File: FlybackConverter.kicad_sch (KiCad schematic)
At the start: 42 parts, among them J1 USB_C_Receptacle_PowerOnly_6P, T1 Transformer_1P_2S, U1 LNK6428K, U2 TPS25820DSST

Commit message: 2024/11/15
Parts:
- removed U1: LNK6428K, Package_SO:PowerIntegrations_eSOP-12B, symbol Regulator_Switching:LNK626PG
- added U1: TNY278G, Package_DIP:PowerIntegrations_SMD-8C, symbol Regulator_Switching:TNY278G
- added VR4: P6KE150A, Diode_THT:D_DO-15_P10.16mm_Horizontal, symbol Device:D_Zener
- C6: value 470p -> 10nF
- R11: value 200k -> 1k
- R3: value 150 -> 100
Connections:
- net PRI: now also VR4.2 (A); no longer R11.1
- net at R6.2, R7.1, TP4.1: now also U1.1 (EN/UV)
- net at C2.2, C7.2, C8.2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: now also U1.5 (S), U1.6 (S), U1.7 (S), U1.8 (S)
- net at D2.1 (K), R3.2: now also R11.2
- net at D2.2 (A), T1.7 (AB): now also U1.4 (D)
- net at C6.2, R3.1: no longer R11.2
- net at C7.1, R8.1: now also U1.2 (BP/M)
- new net: R11.1, VR4.1 (K)
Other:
- moved on the sheet: C7, R11

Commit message: 途中
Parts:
- removed R7: 10k, Resistor_SMD:R_0603_1608Metric, symbol Device:R
- removed TP3, TP4: TestPoint, TestPoint:TestPoint_Loop_D1.80mm_Drill1.0mm_Beaded, symbol Connector:TestPoint
- added C10: 33u, symbol Device:C_Polarized
- added U3: TLP291, Package_SO:SOIC-4_4.55x2.6mm_P1.27mm, symbol Isolator:TLP291
- R5: value 2.4 -> 47
- R6: value 42.2 -> 1; footprint Resistor_SMD:R_0603_1608Metric -> (none)
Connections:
- net at U1.1 (EN/UV): now also U3.4; no longer R6.2
- net at C2.2, C7.2, C8.2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: now also C10.2, U3.3
- net at C8.1, R8.2: now also R5.2; no longer D3.1 (K)
- net at D3.2 (A): now also R6.2; no longer R5.2
- net FB: no longer names the net of R6.1, T1.4 (SB)
- net FB: no longer R5.1
- new net: C10.1, D3.1 (K), R5.1
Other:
- moved on the sheet: R5

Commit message: 回路修正
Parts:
- added D4: 3.9V, Diode_SMD:D_SOD-323, symbol Device:D_Zener
- added R7: 390, Resistor_SMD:R_0603_1608Metric, symbol Device:R
- added TP10: 5V, TestPoint:TestPoint_Loop_D1.80mm_Drill1.0mm_Beaded, symbol Connector:TestPoint
- added TP11: EN/UV, TestPoint:TestPoint_Loop_D1.80mm_Drill1.0mm_Beaded, symbol Connector:TestPoint
- added TP12: BP, TestPoint:TestPoint_Loop_D1.80mm_Drill1.0mm_Beaded, symbol Connector:TestPoint
- added TP13, TP14: GND, TestPoint:TestPoint_Loop_D1.80mm_Drill1.0mm_Beaded, symbol Connector:TestPoint
- added TP3: BP/M, TestPoint:TestPoint_Loop_D1.80mm_Drill1.0mm_Beaded, symbol Connector:TestPoint
- added TP4: EN, TestPoint:TestPoint_Loop_D1.80mm_Drill1.0mm_Beaded, symbol Connector:TestPoint
- added TP9: DRAIN, TestPoint:TestPoint_Loop_D1.80mm_Drill1.0mm_Beaded, symbol Connector:TestPoint
- C10: footprint (none) -> Capacitor_THT:CP_Radial_D5.0mm_P2.50mm
- C7: value 1u -> 100n
- C8: value 10u -> 2.2n; footprint Capacitor_SMD:C_1206_3216Metric -> Capacitor_THT:C_Disc_D10.5mm_W5.0mm_P10.00mm
- R6: value 1 -> Resistor_SMD:R_0603_1608Metric; footprint (none) -> Resistor_THT:R_Axial_DIN0207_L6.3mm_D2.5mm_P7.62mm_Horizontal
- R8: value 2.37k -> 8.06k
- renumbered VR4 to VR1
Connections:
- net 5V: now also TP10.1
- net FL2: now also C8.2, U3.2
- net PRI: now also C8.1
- net at C10.2, C2.2, C7.2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: now also TP13.1, TP14.1; no longer C8.2
- net DRAIN: now reaches D2.2 (A), T1.7 (AB), U1.4 (D)
- net DRAIN: now also TP9.1
- net EN: now reaches C3.1, C5.2, D1.1 (K), L1.1
- net EN: now also D4.1 (K)
- net at R6.1, T1.4 (SB): now also TP12.1
- net at C7.1, U1.2 (BP/M): now also R8.2, TP3.1; no longer R8.1
- net at U3.1: now also R7.2
- net at U1.1 (EN/UV), U3.4: now also TP11.1
- new net: R5.2, R8.1
- new net: D4.2 (A), R7.1, TP4.1

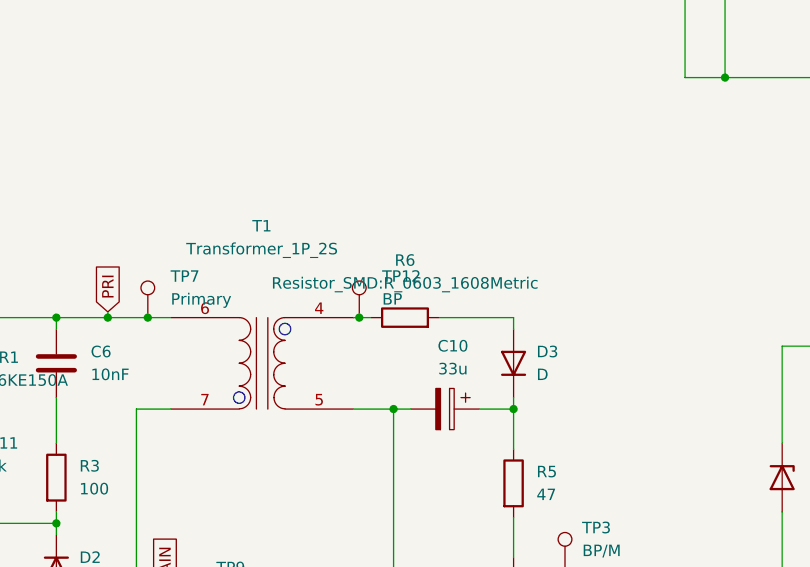
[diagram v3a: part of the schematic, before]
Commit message: TP以外大体配置できた #10
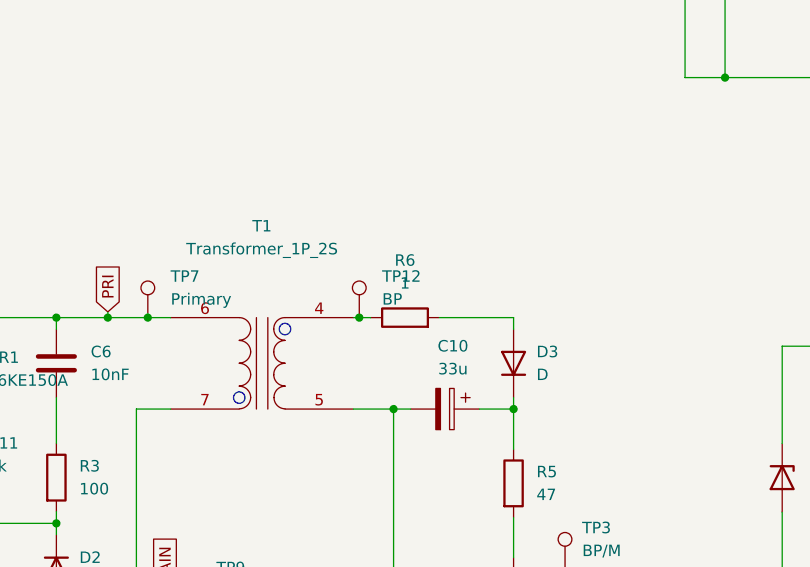
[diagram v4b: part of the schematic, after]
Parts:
- R6: value Resistor_SMD:R_0603_1608Metric -> 1; footprint Resistor_THT:R_Axial_DIN0207_L6.3mm_D2.5mm_P7.62mm_Horizontal -> Resistor_SMD:R_0603_1608Metric
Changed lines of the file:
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@@
       (effects (font (size 1.27 1.27)))
     )
-    (property "Value" "Resistor_SMD:R_0603_1608Metric" (at 136.525 92.71 90)
+    (property "Value" "1" (at 136.525 92.71 90)
       (effects (font (size 1.27 1.27)))
     )
-    (property "Footprint" "Resistor_THT:R_Axial_DIN0207_L6.3mm_D2.5mm_P7.62mm_Horizontal" (at 136.525 98.298 90)
+    (property "Footprint" "Resistor_SMD:R_0603_1608Metric" (at 136.525 98.298 90)
       (effects (font (size 1.27 1.27)) hide)
     )

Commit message: TP配置
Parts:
- added TP15: GND, TestPoint:TestPoint_Loop_D1.80mm_Drill1.0mm_Beaded, symbol Connector:TestPoint
- TP1, TP2: value TestPoint -> AC IN
- TP5: value TestPoint -> SEC
- TP6: value TestPoint -> GND
- TP7: value Primary -> PRI
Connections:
- net FL2: now also TP15.1
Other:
- moved on the sheet: TP6
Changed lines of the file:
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@@
   (junction (at 151.765 58.42) (diameter 0) (color 0 0 0 0)
   )
-  (junction (at 91.44 58.42) (diameter 0) (color 0 0 0 0)
+  (junction (at 107.315 58.42) (diameter 0) (color 0 0 0 0)
   )
   (junction (at 77.47 96.52) (diameter 0) (color 0 0 0 0)
@@
   (junction (at 64.77 96.52) (diameter 0) (color 0 0 0 0)
   )
+  (junction (at 100.965 58.42) (diameter 0) (color 0 0 0 0)
+  )
   (junction (at 148.59 106.68) (diameter 0) (color 0 0 0 0)
   )
@@
     (stroke (width 0) (type default))
   )
-  (wire (pts (xy 91.44 58.42) (xy 125.73 58.42))
-    (stroke (width 0) (type default))
-  )
   (wire (pts (xy 220.98 69.85) (xy 228.6 69.85))
     (stroke (width 0) (type default))
@@
     (stroke (width 0) (type default))
   )
-  (wire (pts (xy 85.09 58.42) (xy 91.44 58.42))
+  (wire (pts (xy 85.09 58.42) (xy 100.965 58.42))
     (stroke (width 0) (type default))
   )
@@
     (stroke (width 0) (type default))
   )
+  (wire (pts (xy 107.315 58.42) (xy 125.73 58.42))
+    (stroke (width 0) (type default))
+  )
   (wire (pts (xy 87.63 106.045) (xy 87.63 107.95))
     (stroke (width 0) (type default))
@@
   )
   (wire (pts (xy 97.79 119.38) (xy 97.79 120.65))
+    (stroke (width 0) (type default))
+  )
+  (wire (pts (xy 100.965 58.42) (xy 107.315 58.42))
     (stroke (width 0) (type default))
   )
@@
       (effects (font (size 1.27 1.27)) (justify right))
     )
-    (property "Value" "TestPoint" (at 36.83 143.002 0)
+    (property "Value" "AC IN" (at 36.83 143.002 0)
       (effects (font (size 1.27 1.27)) (justify right))
     )
@@
       (effects (font (size 1.27 1.27)) (justify left))
     )
-    (property "Value" "TestPoint" (at 93.345 46.228 0)
+    (property "Value" "SEC" (at 93.345 46.228 0)
       (effects (font (size 1.27 1.27)) (justify left))
     )
@@
         (path "/f7ad8aa8-e3ae-4e7c-846c-9c0c6caa5ffd"
           (reference "R11") (unit 1)
+        )
+      )
+    )
+  )
+  (symbol (lib_id "Connector:TestPoint") (at 107.315 58.42 0) (unit 1)
+    (in_bom yes) (on_board yes) (dnp no) (fields_autoplaced)
+    (property "Reference" "TP15" (at 109.855 53.848 0)
+      (effects (font (size 1.27 1.27)) (justify left))
+    )
+    (property "Value" "GND" (at 109.855 56.388 0)
+      (effects (font (size 1.27 1.27)) (justify left))
+    )
+    (property "Footprint" "TestPoint:TestPoint_Loop_D1.80mm_Drill1.0mm_Beaded" (at 112.395 58.42 0)
+      (effects (font (size 1.27 1.27)) hide)
+    )
+    (property "Datasheet" "~" (at 112.395 58.42 0)
+      (effects (font (size 1.27 1.27)) hide)
+    )
+    (pin "1")
+    (instances
+      (project "FlybackConverter"
+        (path "/f7ad8aa8-e3ae-4e7c-846c-9c0c6caa5ffd"
+          (reference "TP15") (unit 1)
         )
       )
@@
       (effects (font (size 1.27 1.27)) (justify right))
     )
-    (property "Value" "TestPoint" (at 22.86 143.002 0)
+    (property "Value" "AC IN" (at 22.86 143.002 0)
       (effects (font (size 1.27 1.27)) (justify right))
     )
@@
     )
   )
-  (symbol (lib_id "Connector:TestPoint") (at 91.44 58.42 0) (unit 1)
-    (in_bom yes) (on_board yes) (dnp no) (fields_autoplaced)
-    (property "Reference" "TP6" (at 93.98 53.848 0)
-      (effects (font (size 1.27 1.27)) (justify left))
-    )
-    (property "Value" "TestPoint" (at 93.98 56.388 0)
-      (effects (font (size 1.27 1.27)) (justify left))
-    )
-    (property "Footprint" "TestPoint:TestPoint_Loop_D1.80mm_Drill1.0mm_Beaded" (at 96.52 58.42 0)
-      (effects (font (size 1.27 1.27)) hide)
-    )
-    (property "Datasheet" "~" (at 96.52 58.42 0)
+  (symbol (lib_id "Connector:TestPoint") (at 100.965 58.42 0) (unit 1)
+    (in_bom yes) (on_board yes) (dnp no) (fields_autoplaced)
+    (property "Reference" "TP6" (at 103.505 53.848 0)
+      (effects (font (size 1.27 1.27)) (justify left))
+    )
+    (property "Value" "GND" (at 103.505 56.388 0)
+      (effects (font (size 1.27 1.27)) (justify left))
+    )
+    (property "Footprint" "TestPoint:TestPoint_Loop_D1.80mm_Drill1.0mm_Beaded" (at 106.045 58.42 0)
+      (effects (font (size 1.27 1.27)) hide)
+    )
+    (property "Datasheet" "~" (at 106.045 58.42 0)
       (effects (font (size 1.27 1.27)) hide)
     )
@@
       (effects (font (size 1.27 1.27)) (justify left))
     )
-    (property "Value" "Primary" (at 110.49 94.488 0)
-      (effects (font (size 1.27 1.27)) (justify left))
-    )
+    (property "Value" "PRI" (at 110.49 94.488 0)
+      (effects (font (size 1.27 1.27)) (justify left))
+    )

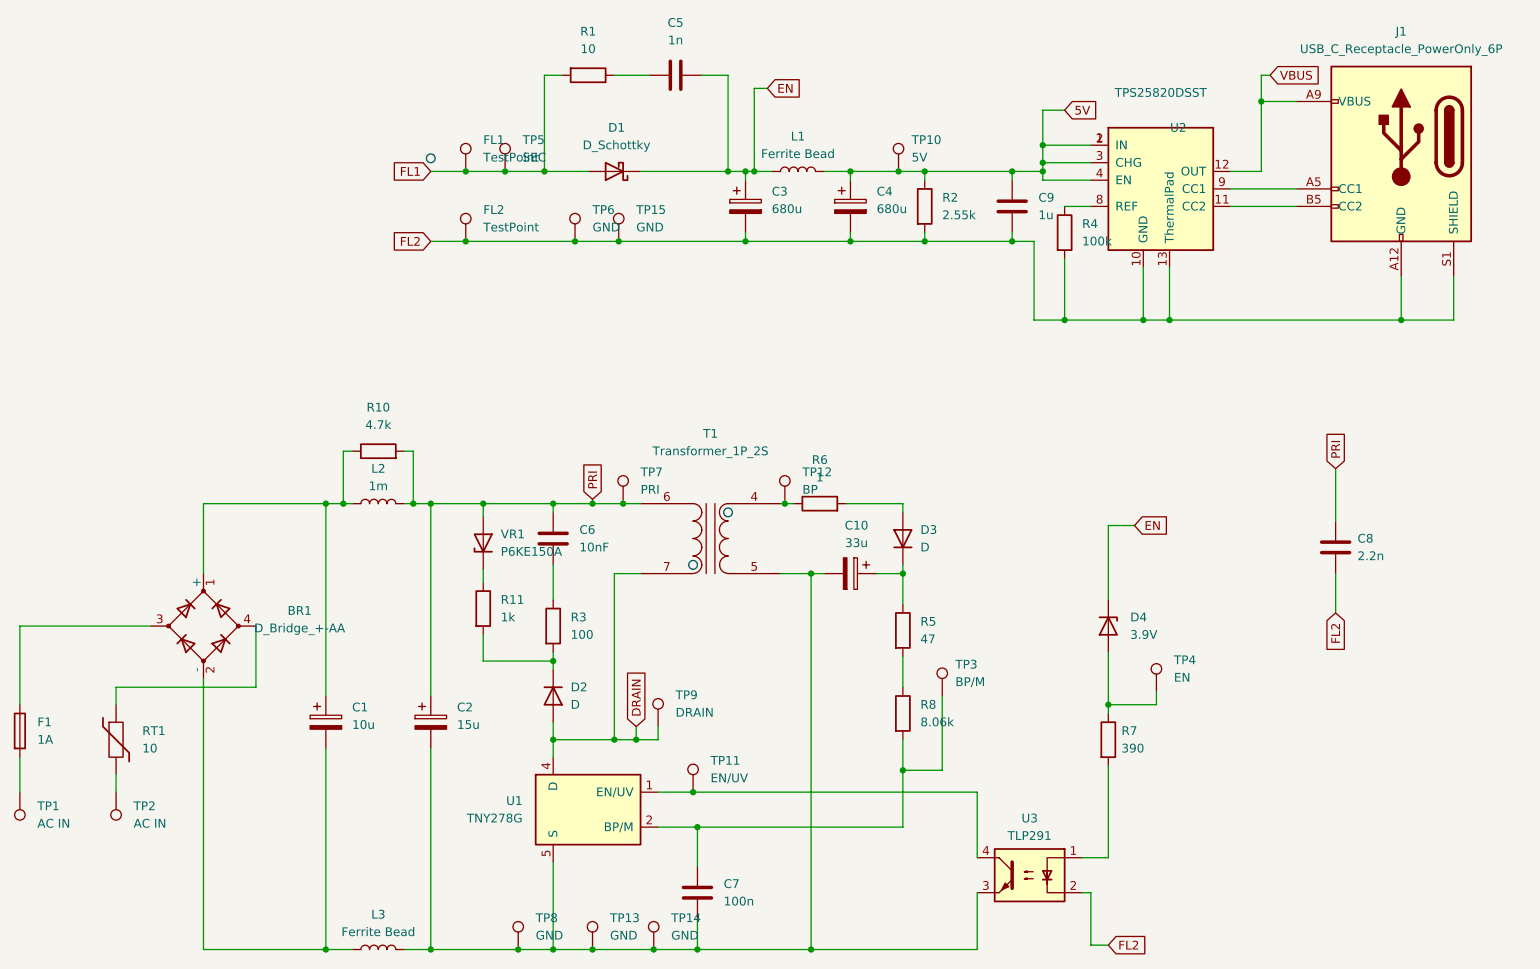
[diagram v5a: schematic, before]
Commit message: 回路図を現物に合わせて修正 #12
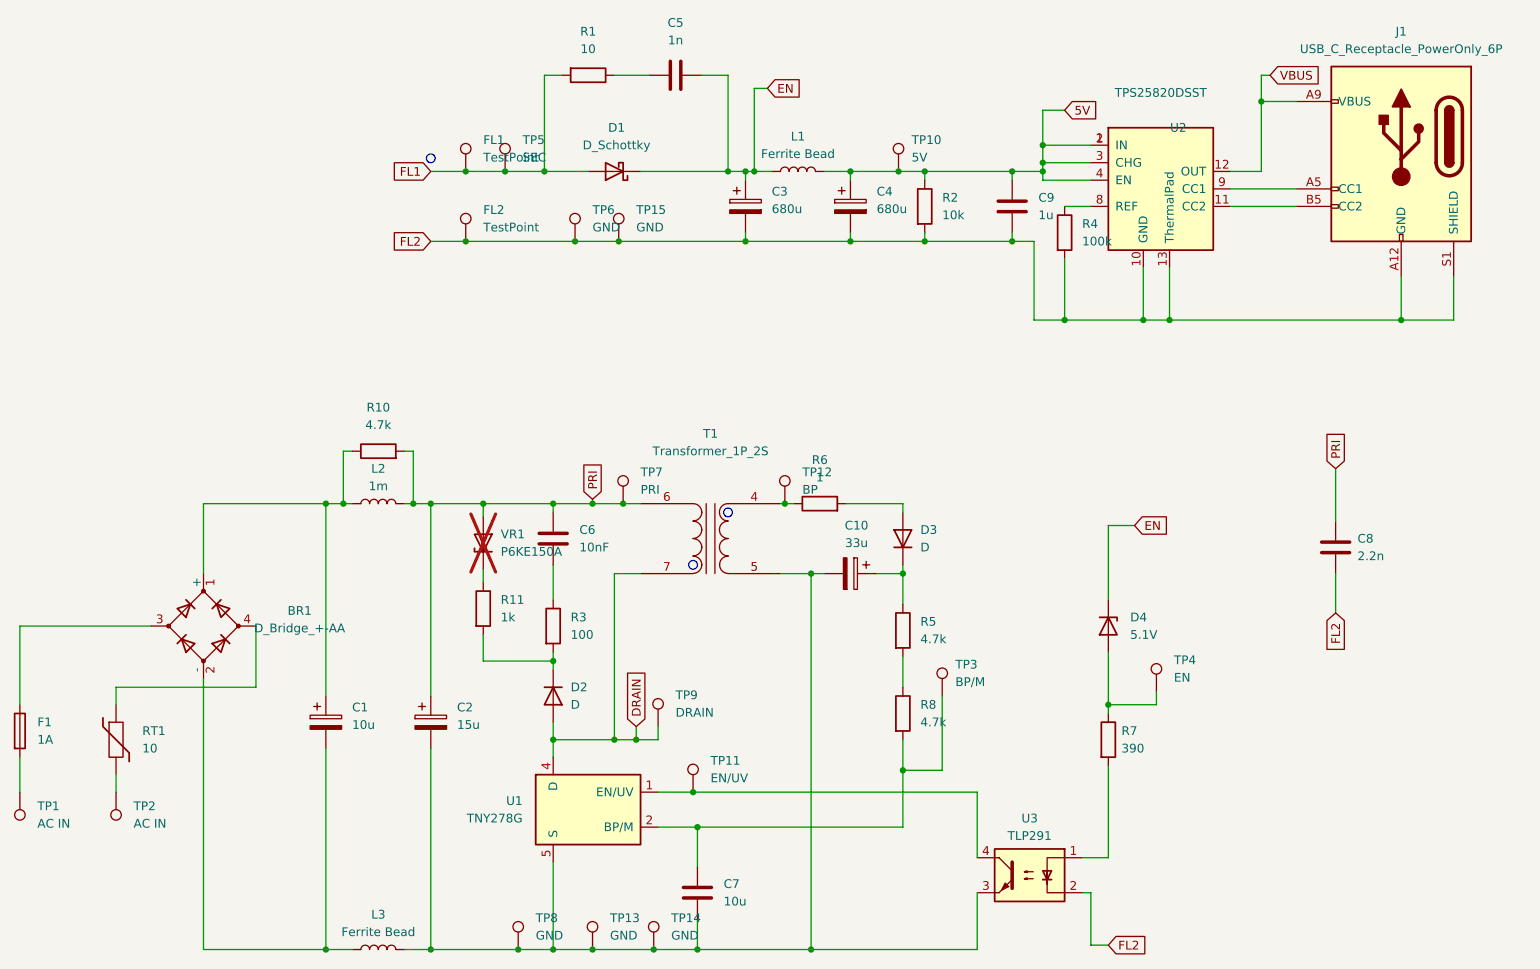
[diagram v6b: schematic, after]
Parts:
- C7: value 100n -> 10u
- D4: value 3.9V -> 5.1V
- R2: value 2.55k -> 10k
- R5: value 47 -> 4.7k
- R8: value 8.06k -> 4.7k
- VR1: now not fitted; now left out of the parts list
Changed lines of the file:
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@@
       (effects (font (size 1.27 1.27)) (justify left))
     )
-    (property "Value" "8.06k" (at 151.13 128.27 0)
+    (property "Value" "4.7k" (at 151.13 128.27 0)
       (effects (font (size 1.27 1.27)) (justify left))
     )
@@
       (effects (font (size 1.27 1.27)) (justify left))
     )
-    (property "Value" "2.55k" (at 154.305 54.61 0)
+    (property "Value" "10k" (at 154.305 54.61 0)
       (effects (font (size 1.27 1.27)) (justify left))
     )
@@
       (effects (font (size 1.27 1.27)) (justify left))
     )
-    (property "Value" "3.9V" (at 181.61 115.57 90)
+    (property "Value" "5.1V" (at 181.61 115.57 90)
       (effects (font (size 1.27 1.27)) (justify left))
     )
@@
       (effects (font (size 1.27 1.27)) (justify left))
     )
-    (property "Value" "47" (at 151.13 116.205 0)
+    (property "Value" "4.7k" (at 151.13 116.205 0)
       (effects (font (size 1.27 1.27)) (justify left))
     )
@@
       (effects (font (size 1.27 1.27)) (justify left))
     )
-    (property "Value" "100n" (at 122.555 154.305 0)
+    (property "Value" "10u" (at 122.555 154.305 0)
       (effects (font (size 1.27 1.27)) (justify left))
     )
@@
   )
   (symbol (lib_id "Device:D_Zener") (at 87.63 102.235 90) (unit 1)
-    (in_bom yes) (on_board yes) (dnp no) (fields_autoplaced)
+    (in_bom no) (on_board yes) (dnp yes) (fields_autoplaced)
     (property "Reference" "VR1" (at 90.17 100.965 90)
       (effects (font (size 1.27 1.27)) (justify right))

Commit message: 細かいパラメータ修正
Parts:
- C6: value 10nF -> 470p
- R11: value 1k -> 200k
- R3: value 100 -> 150
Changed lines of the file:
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@@
       (effects (font (size 1.27 1.27)) (justify left))
     )
-    (property "Value" "1k" (at 90.17 113.03 0)
+    (property "Value" "200k" (at 90.17 113.03 0)
       (effects (font (size 1.27 1.27)) (justify left))
     )
@@
       (effects (font (size 1.27 1.27)) (justify left))
     )
-    (property "Value" "10nF" (at 101.6 102.87 0)
+    (property "Value" "470p" (at 101.6 102.87 0)
       (effects (font (size 1.27 1.27)) (justify left))
     )
@@
       (effects (font (size 1.27 1.27)) (justify left))
     )
-    (property "Value" "100" (at 100.33 115.57 0)
-      (effects (font (size 1.27 1.27)) (justify left))
-    )
+    (property "Value" "150" (at 100.33 115.57 0)
+      (effects (font (size 1.27 1.27)) (justify left))
+    )

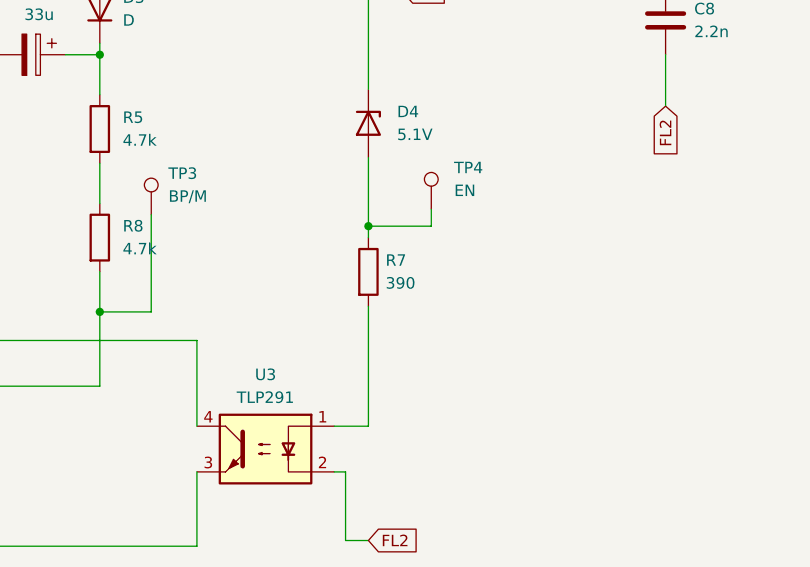
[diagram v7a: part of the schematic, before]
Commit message: R7(FBツェナー部分)抵抗値修正 #12
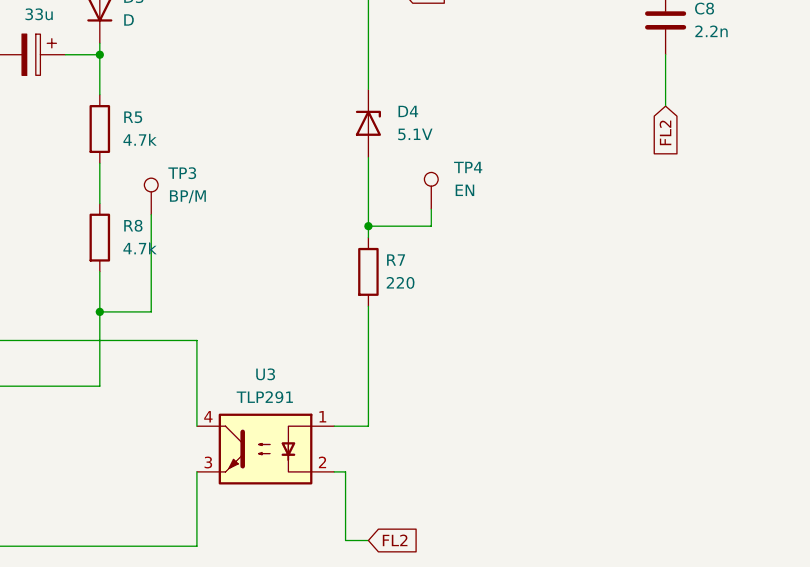
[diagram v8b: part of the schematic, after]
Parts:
- R7: value 390 -> 220
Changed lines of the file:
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@@
       (effects (font (size 1.27 1.27)) (justify left))
     )
-    (property "Value" "390" (at 180.34 132.08 0)
+    (property "Value" "220" (at 180.34 132.08 0)
       (effects (font (size 1.27 1.27)) (justify left))
     )
